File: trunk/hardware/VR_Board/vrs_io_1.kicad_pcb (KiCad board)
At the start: 2 copper layers, 28.6 x 14 mm, 27 parts, among them P103 CONN_5X2, P104 CONN_4, U101 MAX9926/9927

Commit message: VR board
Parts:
- added P105: CONN_01X01, Socket_Strip_Straight_1x01, F.Cu at (215.9, 130.8)
- P103: value CONN_5X2 -> CONN_02X02; footprint PIN_ARRAY_5x2 -> Socket_Strip_Straight_2x02
- moved P103 9.88 mm to (210.8, 130.8), turned to 0 degrees
- moved D802 7.41 mm to (217.2, 121.9), turned to 90 degrees
- moved D801 7.41 mm to (217.2, 125.7), turned to 270 degrees
- moved R113 2.84 mm to (215.3, 125.7)
- moved R114 2.84 mm to (215.3, 121.9)
- moved C103 0.63 mm to (210.2, 127.6)
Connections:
- P103 pad 2: /5V -> /CRANK
- P103 pad 3: /CRANK -> GND
- P103 pad 4: (no net) -> GND
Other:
- board size 28.6 x 14 mm -> 27.3 x 15.9 mm
- board text added: "5V"
- board text added: "VR3"
- board text added: "VR4"
- board text removed: "CAM"
- board text removed: "CRK"

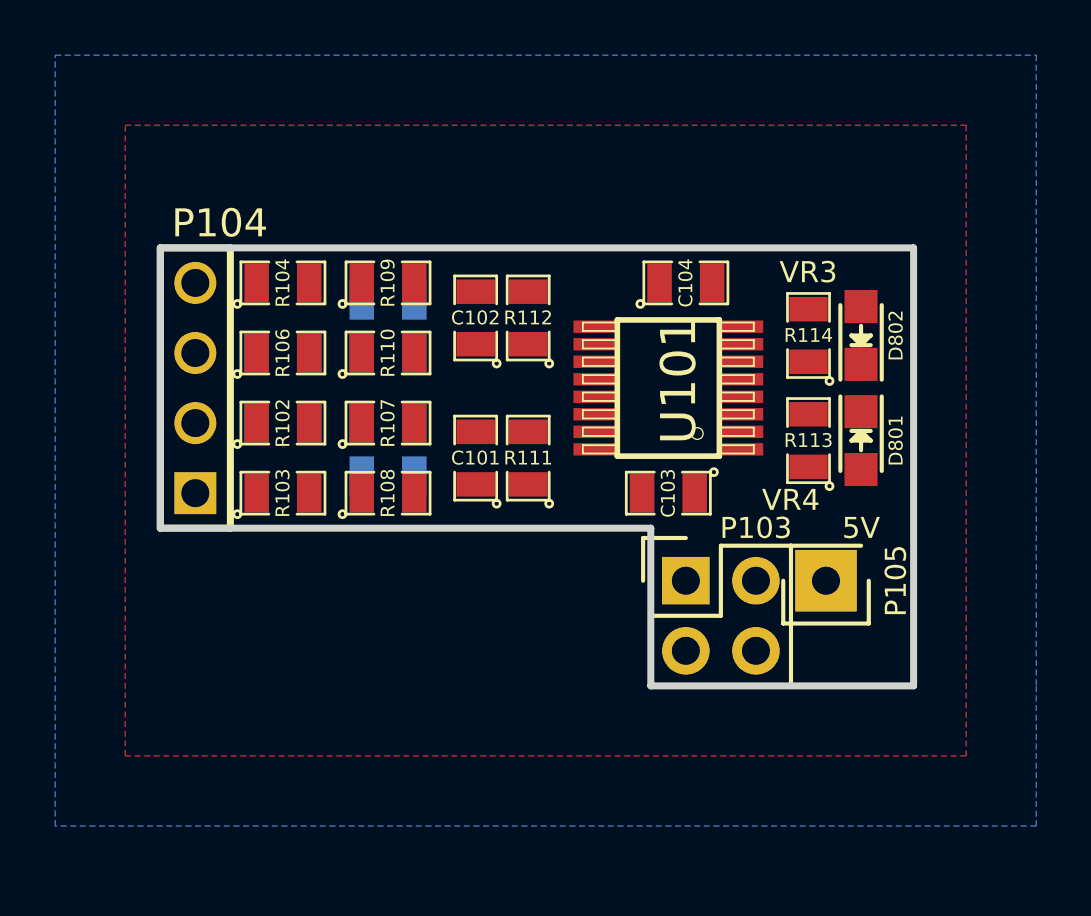
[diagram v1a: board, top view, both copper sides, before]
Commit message: 
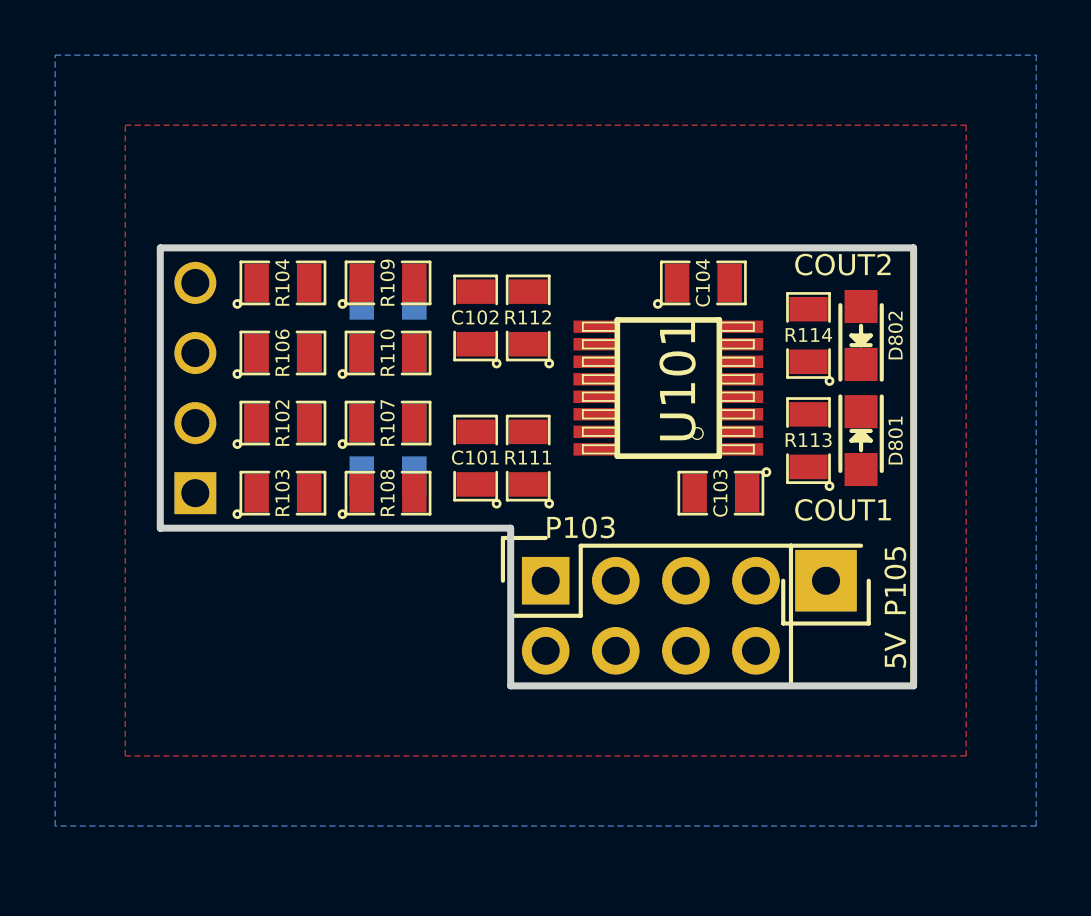
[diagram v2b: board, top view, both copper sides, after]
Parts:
- P103: value CONN_02X02 -> CONN_02X04; footprint Socket_Strip_Straight_2x02 -> Socket_Strip_Straight_2x04
- P104: moved to B.Cu
- moved P103 5.08 mm to (205.7, 130.8)
- moved C103 1.91 mm to (212.1, 127.6)
- moved C104 0.64 mm to (211.5, 120.0)
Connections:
- P103 pad 1: /CAM -> (no net)
- P103 pad 2: /CRANK -> /Cout2
- P103 pad 3: GND -> (no net)
- P103 pad 4: GND -> (no net)
- R113 pad 2: /CRANK -> /Cout1
- R114 pad 1: /CAM -> /Cout2
- U101 pad 4: /CRANK -> /Cout1
- U101 pad 5: /CAM -> /Cout2
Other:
- outline, holes or cut-outs redrawn
- board text added: "COUT1"
- board text added: "COUT2"
- board text removed: "VR3"
- board text removed: "VR4"

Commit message: VR board
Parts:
- moved P103 1.27 mm to (205.7, 132.1)
- moved P105 1.27 mm to (215.9, 132.1)
- moved C103 0.64 mm to (212.1, 127.0)
- moved C104 0.64 mm to (211.5, 119.4)
- moved D801 0.64 mm to (217.2, 125.1)
- moved D802 0.64 mm to (217.2, 121.3)
- moved P104 0.64 mm to (193.0, 123.2)
- moved R102 0.64 mm to (196.2, 124.5)
- moved R103 0.64 mm to (196.2, 127.0)
- moved R104 0.64 mm to (196.2, 119.4)
- moved R106 0.64 mm to (196.2, 121.9)
- moved R107 0.64 mm to (200.0, 124.5)
- moved R108 0.64 mm to (200.0, 127.0)
- moved R109 0.64 mm to (200.0, 119.4)
- moved R110 0.64 mm to (200.0, 121.9)
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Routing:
- net /5V: track 0.00 -> 41.3 mm, vias 0 -> 1
- net GND: track 0.00 -> 25.8 mm, vias 0 -> 6
- net /Cout2: track 0.00 -> 21.7 mm, vias 0 -> 1
- net /Cout1: track 0.00 -> 12.7 mm, vias 0 -> 1
- net Net-(C102-Pad2): track 0.00 -> 7.18 mm
- net Net-(C101-Pad1): track 0.00 -> 7.18 mm
- net Net-(C101-Pad2): track 0.00 -> 6.65 mm
- net Net-(C102-Pad1): track 0.00 -> 6.65 mm
- net Net-(R141-Pad2): track 0.00 -> 4.60 mm
- net Net-(R137-Pad2): track 0.00 -> 4.60 mm
- net /CRK2-: track 0.00 -> 4.44 mm
- net /CAM-: track 0.00 -> 4.44 mm
- net /CRK2+: track 0.00 -> 2.22 mm
- net /CAM+: track 0.00 -> 2.22 mm
- net Net-(D802-Pad2): track 0.00 -> 1.94 mm
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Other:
- board size 27.3 x 15.9 mm -> 27.3 x 17.8 mm
- net class Default: clearance 0.1524 -> 0.1778
- rule trace_clearance: 0.1524 -> 0.1778
